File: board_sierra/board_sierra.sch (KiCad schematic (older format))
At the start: 11 parts

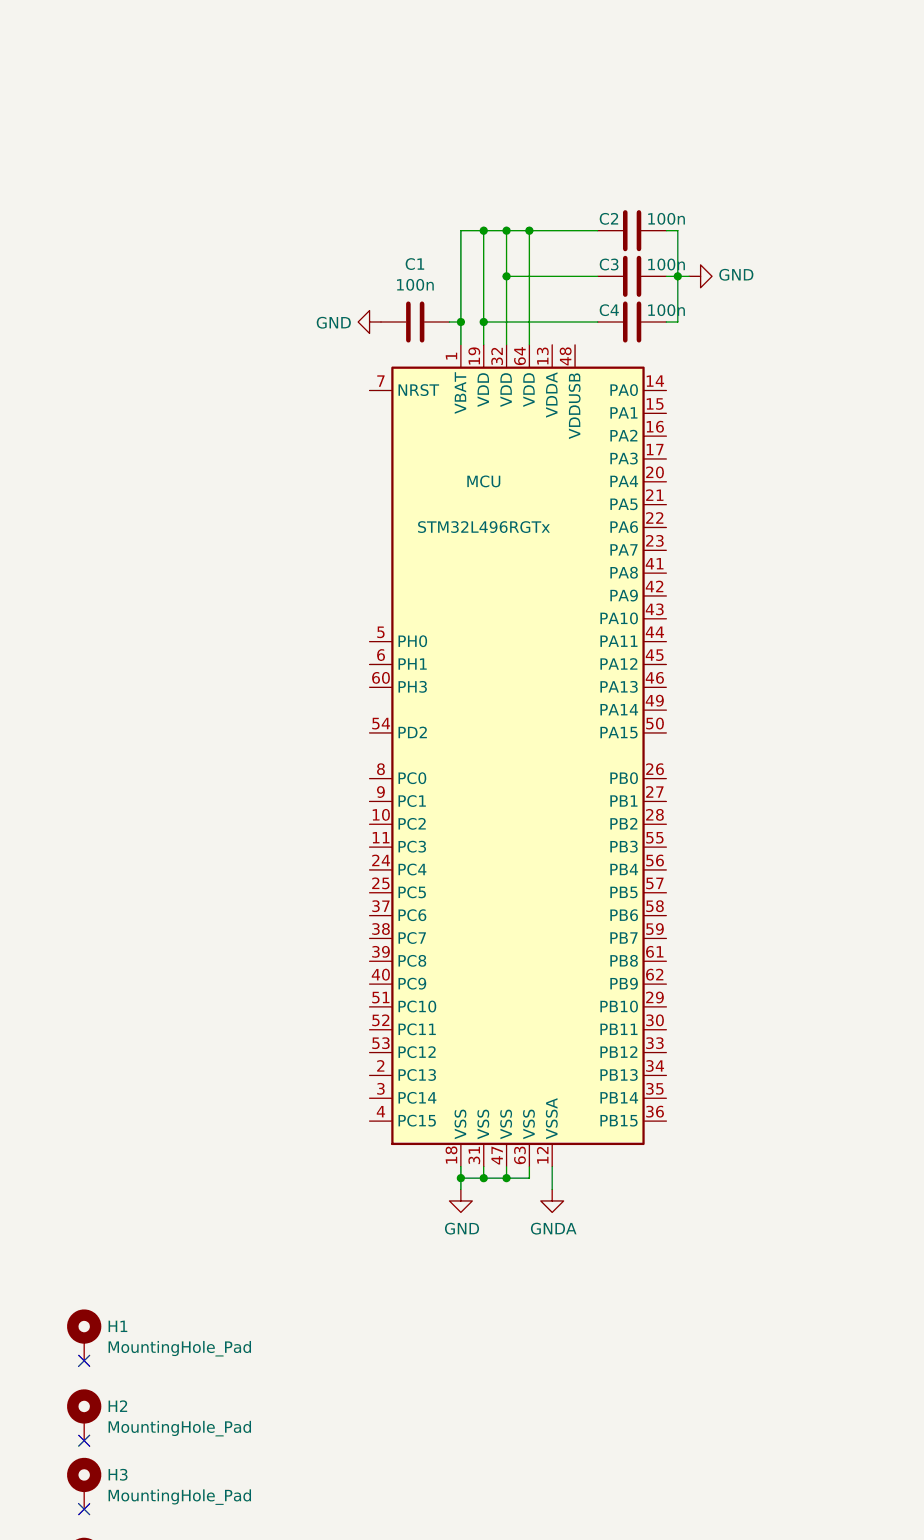
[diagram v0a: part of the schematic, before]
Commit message: supply input, LSE crystal
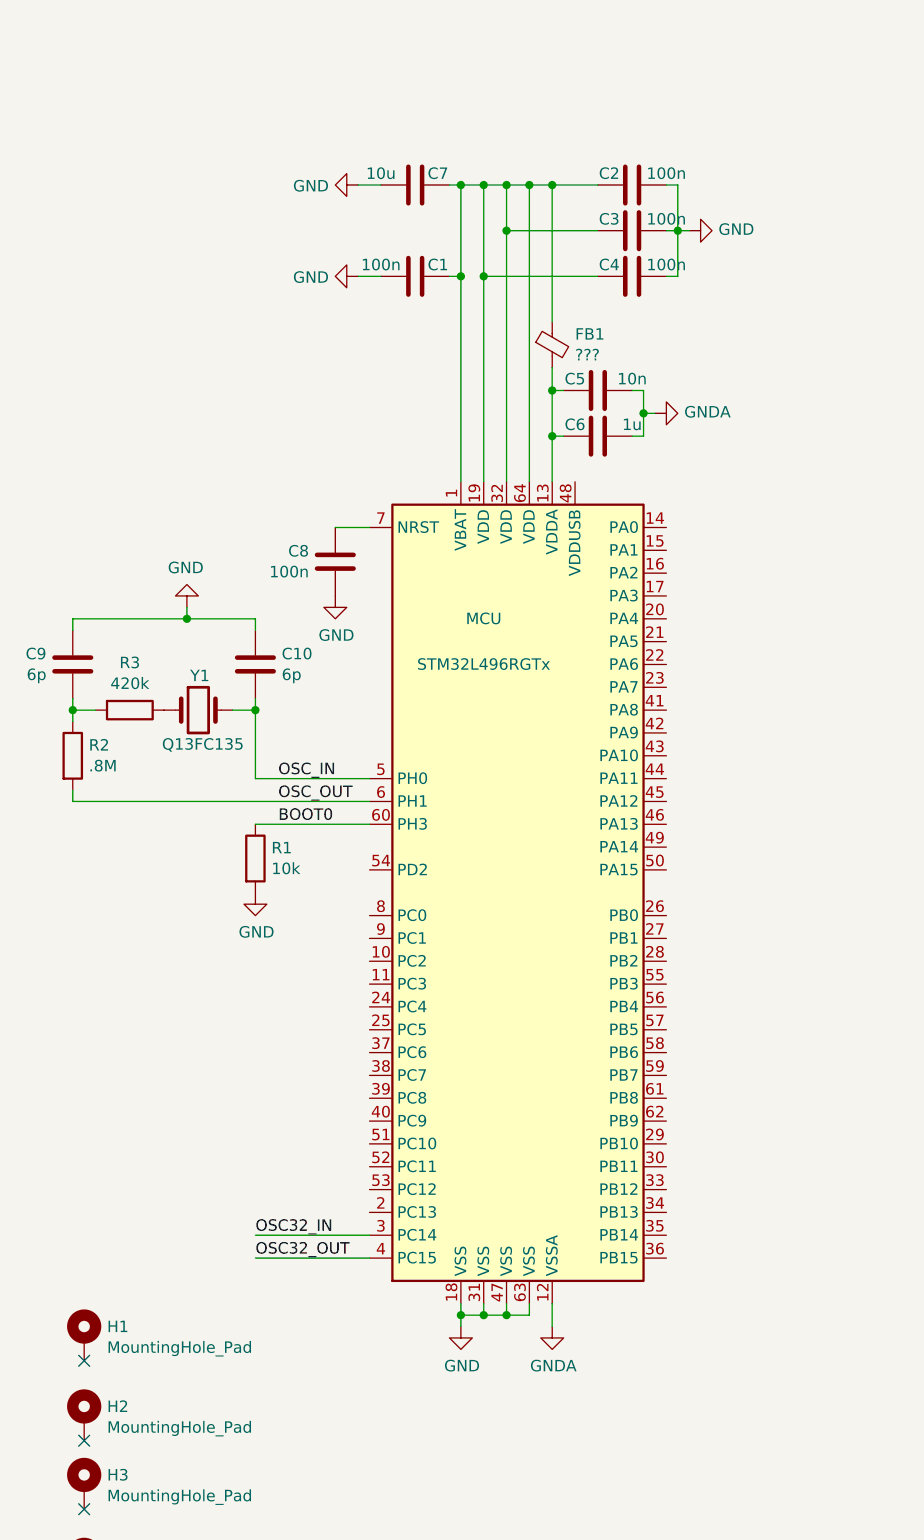
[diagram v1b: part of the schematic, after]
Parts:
- added C10, C9: 6p, symbol Device:C
- added C5: 10n, symbol Device:C
- added C6: 1u, symbol Device:C
- added C7: 10u, symbol Device:C
- added C8: 100n, symbol Device:C
- added FB1: ???, symbol Device:Ferrite_Bead_Small
- added R1: 10k, symbol Device:R
- added R2: .8M, symbol Device:R
- added R3: 420k, symbol Device:R
- added Y1: Q13FC135, Crystal:Crystal_SMD_3215-2Pin_3.2x1.5mm, symbol Device:Crystal
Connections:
- net labels added: BOOT0, OSC32_IN, OSC32_OUT, OSC_IN, OSC_OUT
- wire segments 66 -> 99
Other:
- moved on the sheet: C1, C2, C3, C4, MCU

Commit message: migration to mouser components
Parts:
- added C11, C12, C13: 100n, Capacitor_SMD:C_0805_2012Metric, symbol Device:C
- added Q1: MUN5111, Package_TO_SOT_SMD:SOT-363_SC-70-6, symbol VST104:MUN5111
- added R4: 1k, Resistor_SMD:R_0805_2012Metric, symbol Device:R
- added R6, R7: 10k, Resistor_SMD:R_0805_2012Metric, symbol Device:R
- added TS1, TS2: SE95, Package_SO:TSSOP-8_3x3mm_P0.65mm, symbol VST104:SE95
- added Y2: SiT2024, Package_TO_SOT_SMD:SOT-23-5, symbol VST104:SiT2024
- C1, C2, C3, C4, C5, C6, C7, C8, FB1: footprint (none) -> Capacitor_SMD:C_0805_2012Metric
- C10, C9: value 6p -> 17p; footprint (none) -> Capacitor_SMD:C_0805_2012Metric
- R1: footprint (none) -> Resistor_SMD:R_0805_2012Metric
- R2: value .8M -> 0.29M; footprint (none) -> Resistor_SMD:R_0805_2012Metric
- R3: value 420k -> 450k; footprint (none) -> Resistor_SMD:R_0805_2012Metric
- Y1: value Q13FC135 -> CM8V-T1A; footprint Crystal:Crystal_SMD_3215-2Pin_3.2x1.5mm -> Crystal:Crystal_SMD_2012-2Pin_2.0x1.2mm
- renumbered MCU to MCU1, H1 to MH1, H2 to MH2, H3 to MH3, H4 to MH4
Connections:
- net labels added: +3V3, CAN1_RX, CAN1_TX, CAN2_RX, CAN2_TX, I2C1_EN, I2C1_SC, I2C1_SD
- wire segments 99 -> 140
- no-connect marks 4 -> 6
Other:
- note added: "Temperature measurement - up to 8 sensors\n"
- moved on the sheet: C1, C2, C3, C4, C5, C6, C7, C8, FB1, MCU1, MH1, MH2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

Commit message: end of the day
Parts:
- added C14, C15, C17, C18: 100n, Capacitor_SMD:C_0805_2012Metric, symbol Device:C
- added J1: Conn_01x08, VST104_footprints:5014610891, symbol Connector_Generic:Conn_01x08
- added R7, R8: 120, Resistor_SMD:R_0805_2012Metric, symbol Device:R
- added SW1: SW_Push_Dual, VST104_footprints:EVPBB0AAB000, symbol Switch:SW_Push_Dual
- added U1, U2: MCP2542, Package_SO:SOIC-8_3.9x4.9mm_P1.27mm, symbol VST104:MCP2542
- renumbered R6 to R5, R7 to R6
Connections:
- net labels added: CAN1_EN, CAN2_EN, NRST, OSC_EN, SW_CLK, SW_DIO, SW_O, USART1_RX, USART1_TX
- net labels removed: OSC_OUT
- wire segments 140 -> 232
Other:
- note added: "CAN FD transceiver for both channels"
- note added: "LSE and HSE clock sources"
- note added: "Program and SW debug"
- moved on the sheet: C1, C10, C11, C12, C13, C2, C3, C4, C5, C6, C7, C8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

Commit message: update before consultation
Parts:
- added R9: 10k, Resistor_SMD:R_0805_2012Metric, symbol Device:R
- FB1: footprint Capacitor_SMD:C_0805_2012Metric -> (none)
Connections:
- net labels added: +BATT
- net labels removed: VBAT
- wire segments 232 -> 235
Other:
- note added: "KS_C"
- note added: "KS_NC"
- note added: "KS_NO"
- note added: "LibreCube main headers"
- note added: "Mounting holes pads"
- note added: "RBF_C"
- note added: "RBF_NC"
- note added: "RBF_NO"
- note removed: "KS: C"
- note removed: "KS: NC"
- note removed: "KS: NO"
- note removed: "RBF: C"
- note removed: "RBF: NC"
- note removed: "RBF: NO"
- moved on the sheet: C1, C10, C11, C12, C13, C14, C15, C17, C18, C2, C3, C4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

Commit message: update to AEC-Q100 level 1
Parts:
- removed Q1: MUN5111, Package_TO_SOT_SMD:SOT-363_SC-70-6, symbol VST104:MUN5111
- removed TS1, TS2: SE95, Package_SO:TSSOP-8_3x3mm_P0.65mm, symbol VST104:SE95
- removed U1, U2: MCP2542, Package_SO:SOIC-8_3.9x4.9mm_P1.27mm, symbol VST104:MCP2542
- removed Y2: SiT2024, Package_TO_SOT_SMD:SOT-23-5, symbol VST104:SiT2024
- added L1: 10u, Inductor_SMD:L_0805_2012Metric, symbol Device:L
- added TS1, TS2: MCP9804, Package_DFN_QFN:DFN-8-1EP_3x2mm_P0.5mm_EP1.75x1.45mm, symbol VST104:MCP9804
- added U1, U2: TCAN1051, Package_SON:WSON-8-1EP_3x3mm_P0.5mm_EP1.6x2.0mm, symbol VST104:TCAN1051
- added Y2: SiT8924, Crystal:Crystal_SMD_2016-4Pin_2.0x1.6mm, symbol VST104:SiT8924
- FB1: footprint (none) -> Inductor_SMD:L_0805_2012Metric
- R3: value 450k -> 280k
- Y1: value CM8V-T1A -> ABS07AIG; footprint Crystal:Crystal_SMD_2012-2Pin_2.0x1.2mm -> Crystal:Crystal_SMD_3215-2Pin_3.2x1.5mm
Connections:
- wire segments 235 -> 225
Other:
- moved on the sheet: C12, C13, C5, C6, FB1, R5, R6

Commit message: flash added
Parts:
- added C16, C21: 4n7, Capacitor_SMD:C_0603_1608Metric, symbol Device:C
- added C19, C20, C22, C23: 100p, Capacitor_SMD:C_0603_1608Metric, symbol Device:C
- added C24, C25, C26: 100n, Capacitor_SMD:C_0603_1608Metric, symbol Device:C
- added D1, D2: VCAN16A2, Package_TO_SOT_SMD:SOT-323_SC-70, symbol Device:D_TVS_x2_AAC
- added L2, L3: L, VST104_footprints:CMCH_1210, symbol Device:L_Core_Iron_Coupled_Small_1243
- added R10: 470, Resistor_SMD:R_0603_1608Metric, symbol Device:R
- added R11, R12: 60, Resistor_SMD:R_0603_1608Metric, symbol Device:R
- added R13, R14, R15: 10k, Resistor_SMD:R_0603_1608Metric, symbol Device:R
- added U3, U4, U5: S25FLxL, VST104_footprints:WSON-8-EP-6.0x8.0mm, symbol VST104:S25FLxL
- C1, C10, C11, C12, C13, C14, C15, C17, C18, C2, C3, C4, C5, C6, C7, C8, C9: footprint Capacitor_SMD:C_0805_2012Metric -> Capacitor_SMD:C_0603_1608Metric
- FB1, L1: footprint Inductor_SMD:L_0805_2012Metric -> Inductor_SMD:L_0603_1608Metric
- R1: value 10k -> 1k; footprint Resistor_SMD:R_0805_2012Metric -> Resistor_SMD:R_0603_1608Metric
- R2: value 0.29M -> 280k; footprint Resistor_SMD:R_0805_2012Metric -> Resistor_SMD:R_0603_1608Metric
- R3, R4, R5, R6, R9: footprint Resistor_SMD:R_0805_2012Metric -> Resistor_SMD:R_0603_1608Metric
- R7, R8: value 120 -> 60; footprint Resistor_SMD:R_0805_2012Metric -> Resistor_SMD:R_0603_1608Metric
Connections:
- net +3V3: now also C24.1, C25.1, C26.1, R10.1, R13.1, R14.1, R15.1, U3.8 (VCC), U4.8 (VCC), U5.8 (VCC); no longer J1.1 (Pin_1)
- net CAN_A_H: now also C19.2, L2.2; no longer U1.7 (CANH)
- net CAN_A_L: now also R8.1, C20.2, L2.3; no longer R7.2, U1.6 (CANL)
- net CAN_B_H: now also C22.2, L3.2, R11.1; no longer R8.1, U2.7 (CANH)
- net CAN_B_L: now also C23.2, L3.3, R12.1; no longer R8.2, U2.6 (CANL)
- net GND: now also C16.1, C19.1, C20.1, C21.1, C22.1, C23.1, C24.2, C25.2, C26.2, D1.3 (common), D2.3 (common), U3.4 (VSS), U4.4 (VSS), U5.4 (VSS)
- net OSC32_IN: now also C9.1, Y1.1; no longer C10.2, Y1.2
- net OSC32_OUT: now also R2.2; no longer R2.1
- net at R3.1: now also C10.2, R2.1; no longer Y1.1
- net QSPI_CLK: now reaches MCU1.17 (PA3)
- net QSPI_CLK: now also U3.6 (CLK), U4.6 (CLK), U5.6 (CLK)
- net QSPI_B1_3: now reaches MCU1.22 (PA6)
- net QSPI_B1_3: now also U3.7 (Q3/RST), U4.7 (Q3/RST), U5.7 (Q3/RST)
- net QSPI_B1_2: now reaches MCU1.23 (PA7)
- net QSPI_B1_2: now also U3.3 (Q2/WP), U4.3 (Q2/WP), U5.3 (Q2/WP)
- net QSPI_B1_1: now reaches MCU1.26 (PB0)
- net QSPI_B1_1: now also U3.2 (Q1/SO), U4.2 (Q1/SO), U5.2 (Q1/SO)
- net QSPI_B1_0: now reaches MCU1.27 (PB1)
- net QSPI_B1_0: now also U3.5 (Q0/SI), U4.5 (Q0/SI), U5.5 (Q0/SI)
- new net: R3.2, Y1.2
- new net: D1.1 (A1), L2.1, U1.7 (CANH)
- new net: D1.2 (A2), L2.4, U1.6 (CANL)
- new net: J1.1 (Pin_1), R10.2
- new net: D2.2 (A2), L3.4, U2.6 (CANL)
- new net: D2.1 (A1), L3.1, U2.7 (CANH)
- new net: C21.2, R11.2, R12.2
- new net: C16.2, R7.2, R8.2
- new net QSPI_CS_1: R13.2, U3.1 (CS)
- new net QSPI_CS_2: R14.2, U4.1 (CS)
- new net QSPI_CS_3: R15.2, U5.1 (CS)
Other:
- note added: "Temperature measurement\n"
- note added: "Triple redundant FLASH memory"
- note added: "USART & SW"
- note added: "up to 8\n •••"
- note removed: "Program and SW debug"
- note removed: "Temperature measurement - up to 8 sensors\n"
- moved on the sheet: C10, C11, C12, C13, C14, C15, C17, C18, C9, H1, H2, J1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

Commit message: night update
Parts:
- removed MCU1: STM32L496RGTx, Package_QFP:LQFP-64_10x10mm_P0.5mm, symbol MCU_ST_STM32L4:STM32L496RGTx
- removed SW1: SW_Push_Dual, VST104_footprints:EVPBB0AAB000, symbol Switch:SW_Push_Dual
- removed U3, U4, U5: S25FLxL, VST104_footprints:WSON-8-EP-6.0x8.0mm, symbol VST104:S25FLxL
- added C27, C28, C29, C30, C31, C32, C33, C34, C35, C36, C37, C38, C39, C41, C42, C43, C45: 100n, Capacitor_SMD:C_0603_1608Metric, symbol Device:C
- added C40, C44, C46: 1u, Capacitor_SMD:C_0603_1608Metric, symbol Device:C
- added C47, C48, C49, C50, C51, C52, C53, C54, C55, C56, C? (x4): 100n, symbol Device:C_Small
- added M1, M2, M3: CY15B102Q, Package_SO:SOIC-8_5.275x5.275mm_P1.27mm, symbol VST104:memory
- added M4, M5, M6: S25FLxL, VST104_footprints:WSON-8-EP-6.0x8.0mm, symbol board_sierra-rescue:S25FLxL-VST104
- added R16, R17, R18: 10k, Resistor_SMD:R_0603_1608Metric, symbol Device:R
- added R19: 200k, symbol Device:R
- added SW1: SW_DPDT_x2, symbol Switch:SW_DPDT_x2
- added SW2: SW_Push_Dual, VST104_footprints:EVPBB0AAB000, symbol Switch:SW_Push_Dual
- added TS2, TS3, TS4, TS5, TS6, TS8: MCP9804, Package_DFN_QFN:DFN-8-1EP_3x2mm_P0.5mm_EP1.75x1.45mm, symbol VST104:MCP9804
- added U3: STM32L496QGIx, Package_BGA:UFBGA-132_7x7mm_Layout12x12_P0.5mm, symbol MCU_ST_STM32L4:STM32L496QGIx
- added U4, U5, U6, U7: ADuM142E, Package_SO:QSOP-16_3.9x4.9mm_P0.635mm, symbol VST104:digital_isolator_4_2x2
- added U8, U9: LSF0102-Q1, Package_SO:VSSOP-8_2.3x2mm_P0.5mm, symbol VST104:level_shifter
- added U? (x2): ADuM141E, Package_SO:QSOP-16_3.9x4.9mm_P0.635mm, symbol VST104:digital_isolator_4_3x1
- R1: value 1k -> 10k
- R9: value 10k -> 200k; footprint Resistor_SMD:R_0603_1608Metric -> (none)
- renumbered TS2 to TS7
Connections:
- net +3V3: now also TS7.5 (A2), TS7.6 (A1), C27.1, C28.1, C29.1, C30.1, C31.1, C32.1, C33.1, C34.1, C35.1, C36.2, C37.2, C38.2, C43.2, C44.2, C45.2, C46.2, C55.2, C56.2, M1.8 (VCC), M2.8 (VCC), M3.8 (VCC), M4.8 (VCC), M5.8 (VCC), M6.8 (VCC), R16.1, R17.1, R18.1, SW1.3 (C), TS2.7 (A0), TS2.8 (VDD), TS3.6 (A1), TS3.8 (VDD), TS4.6 (A1), TS4.7 (A0), TS4.8 (VDD), TS5.5 (A2), TS5.8 (VDD), TS6.5 (A2), TS6.7 (A0), TS6.8 (VDD), TS8.5 (A2), TS8.6 (A1), TS8.7 (A0), TS8.8 (VDD), U3.C11 (VDDUSB), U3.C4 (VDD), U3.E2 (VBAT), U3.G11 (VDD), U3.G12 (VDD), U3.G2 (VDD), U3.G6 (VDD), U3.G7 (VDDIO2), U3.H3 (VDD), U8.2 (VrA), U8.7 (VrB), U9.2 (VrA), U9.7 (VrB); no longer R9.1, TS7.7 (A0)
- net +5V: no longer H2.25 (Pin_25), H2.26 (Pin_26)
- net BOOT0: now also U3.A4 (PH3)
- net CAN1_RX: now also U3.A3 (PB8)
- net CAN1_TX: now also U3.A12 (PA12)
- net CAN2_RX: now also U3.C5 (PB5)
- net CAN2_TX: now also U3.B5 (PB6)
- net GND: now also H1.19 (Pin_19), H1.20 (Pin_20), H2.19 (Pin_19), H2.20 (Pin_20), R9.2, TS7.7 (A0), C27.2, C28.2, C29.2, C30.2, C31.2, C32.2, C33.2, C34.2, C35.2, C36.1, C37.1, C38.1, C43.1, C44.1, C45.1, C46.1, C47.2, C48.2, C49.2, C50.2, C51.2, C52.2, C53.2, C54.2, C55.1, C56.1, C?.2, C?.2, C?.2, C?.2, M1.4 (VSS), M2.4 (VSS), M3.4 (VSS), M4.4 (VSS), M5.4 (VSS), M6.4 (VSS), R19.2, SW1.1 (A), SW2.1, SW2.3, TS2.4 (GND), TS2.5 (A2), TS2.6 (A1), TS2.9 (EP), TS3.4 (GND), TS3.5 (A2), TS3.7 (A0), TS3.9 (EP), TS4.4 (GND), TS4.5 (A2), TS4.9 (EP), TS5.4 (GND), TS5.6 (A1), TS5.7 (A0), TS5.9 (EP), TS6.4 (GND), TS6.6 (A1), TS6.9 (EP), TS8.4 (GND), TS8.9 (EP), U3.D3 (VSS), U3.E3 (VSS), U3.F11 (VSS), U3.F12 (VSS), U3.F2 (VSS), U3.F6 (VSS), U3.F7 (VSS), U4.15 (GND2), U4.2 (GND1), U4.8 (GND1), U4.9 (GND2), U5.15 (GND2), U5.2 (GND1), U5.8 (GND1), U5.9 (GND2), U6.15 (GND2), U6.2 (GND1), U6.8 (GND1), U6.9 (GND2), U7.15 (GND2), U7.2 (GND1), U7.8 (GND1), U7.9 (GND2), U8.1 (GND), U9.1 (GND), U?.15 (GND2), U?.15 (GND2), U?.2 (GND1), U?.2 (GND1), U?.8 (GND1), U?.8 (GND1), U?.9 (GND2), U?.9 (GND2); no longer H1.33 (Pin_33), H1.34 (Pin_34), H2.29 (Pin_29), H2.30 (Pin_30), H2.32 (Pin_32), R1.2, TS7.5 (A2), TS7.6 (A1)
- net GNDA: now also H1.33 (Pin_33), C39.1, C40.1, C41.1, C42.1, U3.J1 (VSSA); no longer H2.31 (Pin_31)
- net I2C1_EN: now also R9.1, U8.8 (EN)
- net NRST: now also SW2.2, SW2.4, U3.H2 (NRST); no longer R9.2
- net OSC32_IN: now also U3.D1 (PC14)
- net OSC32_OUT: now also U3.E1 (PC15)
- net OSC_EN: now also U3.G1 (PH1)
- net OSC_IN: now also U3.F1 (PH0)
- net QSPI_B1_0: now also M1.5 (Q0/SI), M2.5 (Q0/SI), M3.5 (Q0/SI), M4.5 (Q0/SI), M5.5 (Q0/SI), M6.5 (Q0/SI), U3.B7 (PD4), U3.L9 (PE12)
- net QSPI_B1_1: now also M1.2 (Q1/SO), M2.2 (Q1/SO), M3.2 (Q1/SO), M4.2 (Q1/SO), M5.2 (Q1/SO), M6.2 (Q1/SO), U3.A6 (PD5), U3.M5 (PB0)
- net QSPI_B1_2: now also M1.3 (Q2/WP), M2.3 (Q2/WP), M3.3 (Q2/WP), M4.3 (Q2/WP), M5.3 (Q2/WP), M6.3 (Q2/WP), U3.B6 (PD6), U3.J5 (PA7)
- net QSPI_B1_3: now also M1.7 (Q3/RST), M2.7 (Q3/RST), M3.7 (Q3/RST), M4.7 (Q3/RST), M5.7 (Q3/RST), M6.7 (Q3/RST), U3.A5 (PD7), U3.L4 (PA6)
- net QSPI_CLK: now also M1.6 (CLK), M2.6 (CLK), M3.6 (CLK), M4.6 (CLK), M5.6 (CLK), M6.6 (CLK), U3.L3 (PA3)
- net SW_CLK: now also U3.A10 (PA14)
- net SW_DIO: now also U3.A11 (PA13)
- net SW_O: now also U3.A8 (PB3)
- net SPI_2_MOSI: now reaches H2.12 (Pin_12)
- net SPI_2_MOSI: now also U?.14 (OA)
- net SPI_2_CLK: now reaches H2.13 (Pin_13)
- net SPI_2_CLK: now also U?.13 (OB)
- net SPI_2_MISO: now reaches H2.14 (Pin_14)
- net SPI_2_MISO: now also U?.12 (OC)
- net UART_2_TX: now reaches H2.15 (Pin_15)
- net UART_2_TX: now also U7.14 (OA)
- net UART_2_CTS: now reaches H2.16 (Pin_16)
- net UART_2_CTS: now also U7.11 (ID)
- net UART_2_RX: now reaches H2.17 (Pin_17)
- net UART_2_RX: now also U7.12 (IC)
- net UART_2_RTS: now reaches H2.18 (Pin_18)
- net UART_2_RTS: now also U7.13 (OB)
- net UART_RCS_2_TX: now reaches H2.21 (Pin_21)
- net UART_RCS_2_TX: now also U5.14 (OA)
- net UART_RCS_2_CTS: now reaches H2.22 (Pin_22)
- net UART_RCS_2_CTS: now also U5.11 (ID)
- net UART_RCS_2_RX: now reaches H2.23 (Pin_23)
- net UART_RCS_2_RX: now also U5.12 (IC)
- net UART_RCS_2_RTS: now reaches H2.24 (Pin_24)
- net UART_RCS_2_RTS: now also U5.13 (OB)
- net CAN_2_L: now reaches H2.27 (Pin_27)
- net CAN_2_L: now also C23.2, L3.3, R12.1
- net CAN_2_H: now reaches H2.28 (Pin_28)
- net CAN_2_H: now also C22.2, L3.2, R11.1
- net SPI_1_CS1: now reaches H1.11 (Pin_11)
- net SPI_1_CS1: now also U?.11 (ID)
- net SPI_1_MOSI: now reaches H1.12 (Pin_12)
- net SPI_1_MOSI: now also U?.14 (OA)
- net SPI_1_CLK: now reaches H1.13 (Pin_13)
- net SPI_1_CLK: now also U?.13 (OB)
- net SPI_1_MISO: now reaches H1.14 (Pin_14)
- net SPI_1_MISO: now also U?.12 (OC)
- net UART_1_TX: now reaches H1.15 (Pin_15)
- net UART_1_TX: now also U6.14 (OA)
- net UART_1_CTS: now reaches H1.16 (Pin_16)
- net UART_1_CTS: now also U6.11 (ID)
- net UART_1_RX: now reaches H1.17 (Pin_17)
- net UART_1_RX: now also U6.12 (IC)
- net UART_1_RTS: now reaches H1.18 (Pin_18)
- net UART_1_RTS: now also U6.13 (OB)
- net UART_RCS_1_TX: now reaches H1.21 (Pin_21)
- net UART_RCS_1_TX: now also U4.14 (OA)
- net UART_RCS_1_CTS: now reaches H1.22 (Pin_22)
- net UART_RCS_1_CTS: now also U4.11 (ID)
- net UART_RCS_1_RX: now reaches H1.23 (Pin_23)
- net UART_RCS_1_RX: now also U4.12 (IC)
- net UART_RCS_1_RTS: now reaches H1.24 (Pin_24)
- net UART_RCS_1_RTS: now also U4.13 (OB)
- net I2C_1_SCL: now reaches H1.25 (Pin_25)
- net I2C_1_SCL: now also U8.6 (B1)
- net I2C_1_SDA: now reaches H1.26 (Pin_26)
- net I2C_1_SDA: now also U8.5 (B2)
- net CAN_1_H: now reaches H1.27 (Pin_27)
- net CAN_1_H: now also C19.2, L2.2, R7.1
- net CAN_1_L: now reaches H1.28 (Pin_28)
- net CAN_1_L: now also C20.2, L2.3, R8.1
- net SUP_3V3: now reaches H1.29 (Pin_29)
- net SUP_3V3: now also H1.31 (Pin_31)
- net SUP_5V: now reaches H1.30 (Pin_30)
- net SUP_5V: now also H1.32 (Pin_32)
- net CPU_WD_1: now reaches H1.35 (Pin_35)
- net CPU_WD_2: now reaches H1.36 (Pin_36)
- net GLO_KS_1: now reaches H1.37 (Pin_37)
- net GLO_KS_2: now reaches H1.38 (Pin_38)
- net GLO_KS_3: now reaches H1.39 (Pin_39)
- net GLO_KS_4: now reaches H1.40 (Pin_40)
- net +3.3VADC: now reaches C5.2, C6.2, FB1.2
- net +3.3VADC: now also C39.2, C40.2, C41.2, C42.2, U3.L1 (VREF+), U3.M1 (VDDA), U3.M3 (OPAMP1_VINM), U3.M4 (OPAMP2_VINM)
- net +BATT: no longer names the net of H2.45 (Pin_45)
- net +BATT: no longer H2.46 (Pin_46)
- removed net CAN_A_H: C19.2, H1.2 (Pin_2), L2.2, R7.1
- removed net CAN_A_L: C20.2, H1.1 (Pin_1), L2.3, R8.1
- removed net CAN_B_H: C22.2, H2.2 (Pin_2), L3.2, R11.1
- removed net CAN_B_L: C23.2, H2.1 (Pin_1), L3.3, R12.1
- removed net CHARGE: H1.31 (Pin_31), H1.32 (Pin_32)
- net FCL1: no longer names the net of H1.3 (Pin_3)
- net FCL2: no longer names the net of H1.5 (Pin_5)
- net I2C1_SC renamed I2C4_SCL
- net I2C4_SCL: now also TS2.2 (SCL), TS3.2 (SCL), TS4.2 (SCL), TS5.2 (SCL), TS6.2 (SCL), TS8.2 (SCL), U3.H1 (PC0)
- net I2C1_SD renamed I2C4_SDA
- net I2C4_SDA: now also TS2.1 (SDA), TS3.1 (SDA), TS4.1 (SDA), TS5.1 (SDA), TS6.1 (SDA), TS8.1 (SDA), U3.B4 (PB7)
- net LCL1: no longer names the net of H2.3 (Pin_3)
- net LCL2: no longer names the net of H2.5 (Pin_5)
- net LCL3: no longer names the net of H2.7 (Pin_7)
- net LCL4 renamed SPI_2_CS2
- net LCL5 renamed SPI_2_CS1
- net SPI_2_CS1: now also U?.11 (ID)
- net QSPI_CS_1 renamed QSPI_B1_A
- net QSPI_B1_A: now also M1.1 (CS)
- net QSPI_CS_2 renamed QSPI_B1_B
- net QSPI_B1_B: now also M2.1 (CS)
- net QSPI_CS_3 renamed QSPI_B1_C
- net QSPI_B1_C: now also M3.1 (CS)
- net S0 renamed CPU_SELECT
- net CPU_SELECT: no longer H2.33 (Pin_33)
- net S1 renamed GLO_FAULT
- net GLO_FAULT: no longer H2.35 (Pin_35)
- net S2 renamed GLO_KS_5
- net GLO_KS_5: no longer H2.38 (Pin_38)
- net S3 renamed GLO_KS_7
- net GLO_KS_7: no longer H2.40 (Pin_40)
- net S4: no longer names the net of H2.41 (Pin_41)
- net S4: no longer H2.42 (Pin_42)
- net S5: no longer names the net of H2.43 (Pin_43)
- net S5: no longer H2.44 (Pin_44)
- net SEL_PCDU_RT_A: no longer names the net of H1.7 (Pin_7)
- net SEL_PCDU_RT_B renamed SPI_1_CS2
- net USART1_RX renamed UART3_RX
- net UART3_RX: now also U3.C10 (PC11), U6.5 (OC)
- net USART1_TX renamed UART3_TX
- net UART3_TX: now also U3.B11 (PC10), U6.3 (IA)
- new net: R1.2, SW1.2 (B)
- new net: C47.1, U4.1 (VCC1)
- new net: C49.1, U4.16 (VCC2)
- new net: C48.1, U5.1 (VCC1)
- new net: C50.1, U5.16 (VCC2)
- new net: C51.1, U6.1 (VCC1)
- new net: C53.1, U6.16 (VCC2)
- new net: C52.1, U7.1 (VCC1)
- new net: C54.1, U7.16 (VCC2)
- new net: C?.1, U?.16 (VCC2) (x2)
- new net: C?.1, U?.1 (VCC1) (x2)
- new net GLO_KS_6: H2.38 (Pin_38)
- new net GLO_KS_8: H2.40 (Pin_40)
- new net GLO_SYNC: H2.35 (Pin_35)
- new net I2C1_SCL: U8.3 (A1)
- new net I2C1_SDA: U8.4 (A2)
- new net I2C2_EN: R19.1, U9.8 (EN)
- new net I2C2_SCL: U9.3 (A1)
- new net I2C2_SDA: U9.4 (A2)
- new net I2C_2_SCL: H2.25 (Pin_25), U9.6 (B1)
- new net I2C_2_SDA: H2.26 (Pin_26), U9.5 (B2)
- new net QSPI_B2_A: M4.1 (CS), R16.2
- new net QSPI_B2_B: M5.1 (CS), R17.2
- new net QSPI_B2_C: M6.1 (CS), R18.2
- new net SPI1_CLK: U?.4 (IB)
- new net SPI1_CS1: U?.5 (IC)
- new net SPI1_EN: U?.10 (EN2), U?.7 (EN1)
- new net SPI1_MISO: U?.6 (OD)
- new net SPI1_MOSI: U?.3 (IA)
- new net SPI2_CLK: U?.4 (IB)
- new net SPI2_CS1: U?.6 (OD)
- new net SPI2_EN: U?.10 (EN2), U?.7 (EN1)
- new net SPI2_MISO: U?.5 (IC)
- new net SPI2_MOSI: U?.3 (IA)
- new net SUP_3V3_REF: H1.34 (Pin_34)
- new net SUP_5V_REF: H2.33 (Pin_33)
- new net SUP_BAT_1: H2.30 (Pin_30)
- new net SUP_BAT_2: H2.32 (Pin_32)
- new net SUP_UNREG: H2.29 (Pin_29), H2.31 (Pin_31)
- new net UART1_CTS: U4.6 (OD)
- new net UART1_EN: U4.10 (EN2), U4.7 (EN1)
- new net UART1_RST: U4.4 (IB)
- new net UART1_RX: U4.5 (OC)
- new net UART1_TX: U4.3 (IA)
- new net UART2_CTS: U5.6 (OD)
- new net UART2_EN: U5.10 (EN2), U5.7 (EN1)
- new net UART2_RST: U5.4 (IB)
- new net UART2_RX: U5.5 (OC)
- new net UART2_TX: U5.3 (IA)
- new net UART3_CTS: U6.6 (OD)
- new net UART3_EN: U6.10 (EN2), U6.7 (EN1)
- new net UART3_RST: U6.4 (IB)
- new net UART4_CTS: U7.6 (OD)
- new net UART4_EN: U7.10 (EN2), U7.7 (EN1)
- new net UART4_RST: U7.4 (IB)
- new net UART4_RX: U7.5 (OC)
- new net UART4_TX: U7.3 (IA)
- no-connect marks 6 -> 12
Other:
- note added: "Bank 1 : triple redundant F-RAM memory"
- note added: "Bank 2 : triple redundant FLASH memory"
- note added: "CAN FD transceiver and isolator"
- note added: "I2C level shifter and isolator"
- note added: "Radio subs. UART isolator"
- note added: "SPI isolator"
- note added: "UART isolator"
- note removed: "CAN FD transceiver for both channels"
- note removed: "KS_C"
- note removed: "KS_NC"
- note removed: "KS_NO"
- note removed: "RBF_C"
- note removed: "RBF_NC"
- note removed: "RBF_NO"
- note removed: "Triple redundant FLASH memory"
- note removed: "up to 8\n •••"
- moved on the sheet: C1, C10, C11, C12, C13, C14, C15, C16, C17, C18, C19, C2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
